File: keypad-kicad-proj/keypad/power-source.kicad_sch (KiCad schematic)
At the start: 12 parts, among them J1 Screw_Terminal_01x02, Q3 IRF9393TRPBF, U2 TLV75901PDRVT

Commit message: footprints
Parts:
- C1, C2: footprint (none) -> Capacitor_SMD:C_0603_1608Metric
- D22: footprint (none) -> Diode_SMD:D_SOD-123
- Q3: footprint SOIC127P600X175-8N -> PUT_RocketLab_other:SOIC127P600X175-8N
- R1: footprint (none) -> Resistor_SMD:R_0402_1005Metric
- R12, R2, R3: footprint (none) -> Resistor_SMD:R_0805_2012Metric
- R4: footprint (none) -> Resistor_SMD:R_0603_1608Metric
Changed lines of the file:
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@@
       (effects (font (size 1.27 1.27)) (justify left))
     )
-    (property "Footprint" "" (at 130.81 125.73 0)
+    (property "Footprint" "Capacitor_SMD:C_0603_1608Metric" (at 130.81 125.73 0)
       (effects (font (size 1.27 1.27)) hide)
     )
@@
       (effects (font (size 1.27 1.27)) (justify left))
     )
-    (property "Footprint" "" (at 173.99 123.19 0)
+    (property "Footprint" "Resistor_SMD:R_0805_2012Metric" (at 173.99 123.19 0)
       (effects (font (size 1.27 1.27)) hide)
     )
@@
       (effects (font (size 1.27 1.27)) (justify left))
     )
-    (property "Footprint" "" (at 182.88 127 0)
+    (property "Footprint" "Capacitor_SMD:C_0603_1608Metric" (at 182.88 127 0)
       (effects (font (size 1.27 1.27)) hide)
     )
@@
       (effects (font (size 1.27 1.27)) (justify left))
     )
-    (property "Footprint" "" (at 134.62 57.15 0)
+    (property "Footprint" "Resistor_SMD:R_0805_2012Metric" (at 134.62 57.15 0)
       (effects (font (size 1.27 1.27)) hide)
     )
@@
       (effects (font (size 1.27 1.27)))
     )
-    (property "Footprint" "SOIC127P600X175-8N" (at 165.1 141.91 0)
+    (property "Footprint" "PUT_RocketLab_other:SOIC127P600X175-8N" (at 165.1 141.91 0)
       (effects (font (size 1.27 1.27)) (justify left top) hide)
     )
@@
       (effects (font (size 1.27 1.27)) (justify left))
     )
-    (property "Footprint" "" (at 134.62 64.77 0)
+    (property "Footprint" "Resistor_SMD:R_0603_1608Metric" (at 134.62 64.77 0)
       (effects (font (size 1.27 1.27)) hide)
     )
@@
       (effects (font (size 1.27 1.27)) (justify left))
     )
-    (property "Footprint" "" (at 173.99 128.27 0)
+    (property "Footprint" "Resistor_SMD:R_0402_1005Metric" (at 173.99 128.27 0)
       (effects (font (size 1.27 1.27)) hide)
     )
@@
       (effects (font (size 1.27 1.27)) (justify right))
     )
-    (property "Footprint" "" (at 172.72 52.07 90)
+    (property "Footprint" "Diode_SMD:D_SOD-123" (at 172.72 52.07 90)
       (effects (font (size 1.27 1.27)) hide)
     )
@@
       (effects (font (size 1.27 1.27)) (justify left))
     )
-    (property "Footprint" "" (at 172.72 63.5 0)
-      (effects (font (size 1.27 1.27)) hide)
-    )
+    (property "Footprint" "Resistor_SMD:R_0805_2012Metric" (at 172.72 63.5 0)
+      (effects (font (size 1.27 1.27)) hide)
+    )

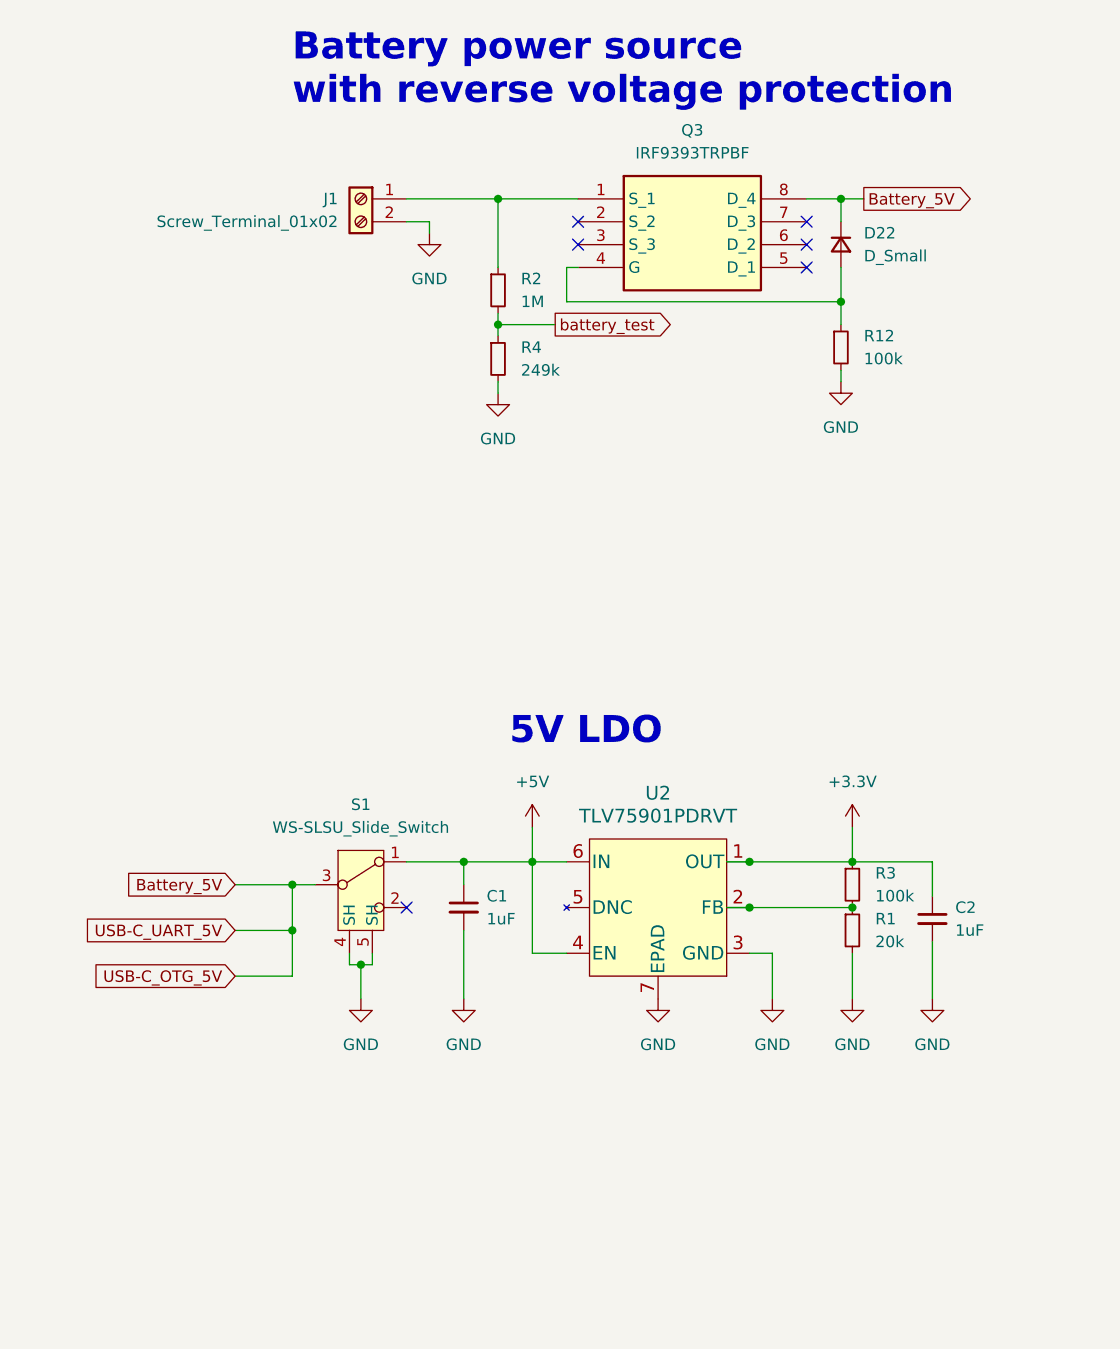
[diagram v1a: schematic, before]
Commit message: add all footprints & move libs to project specific
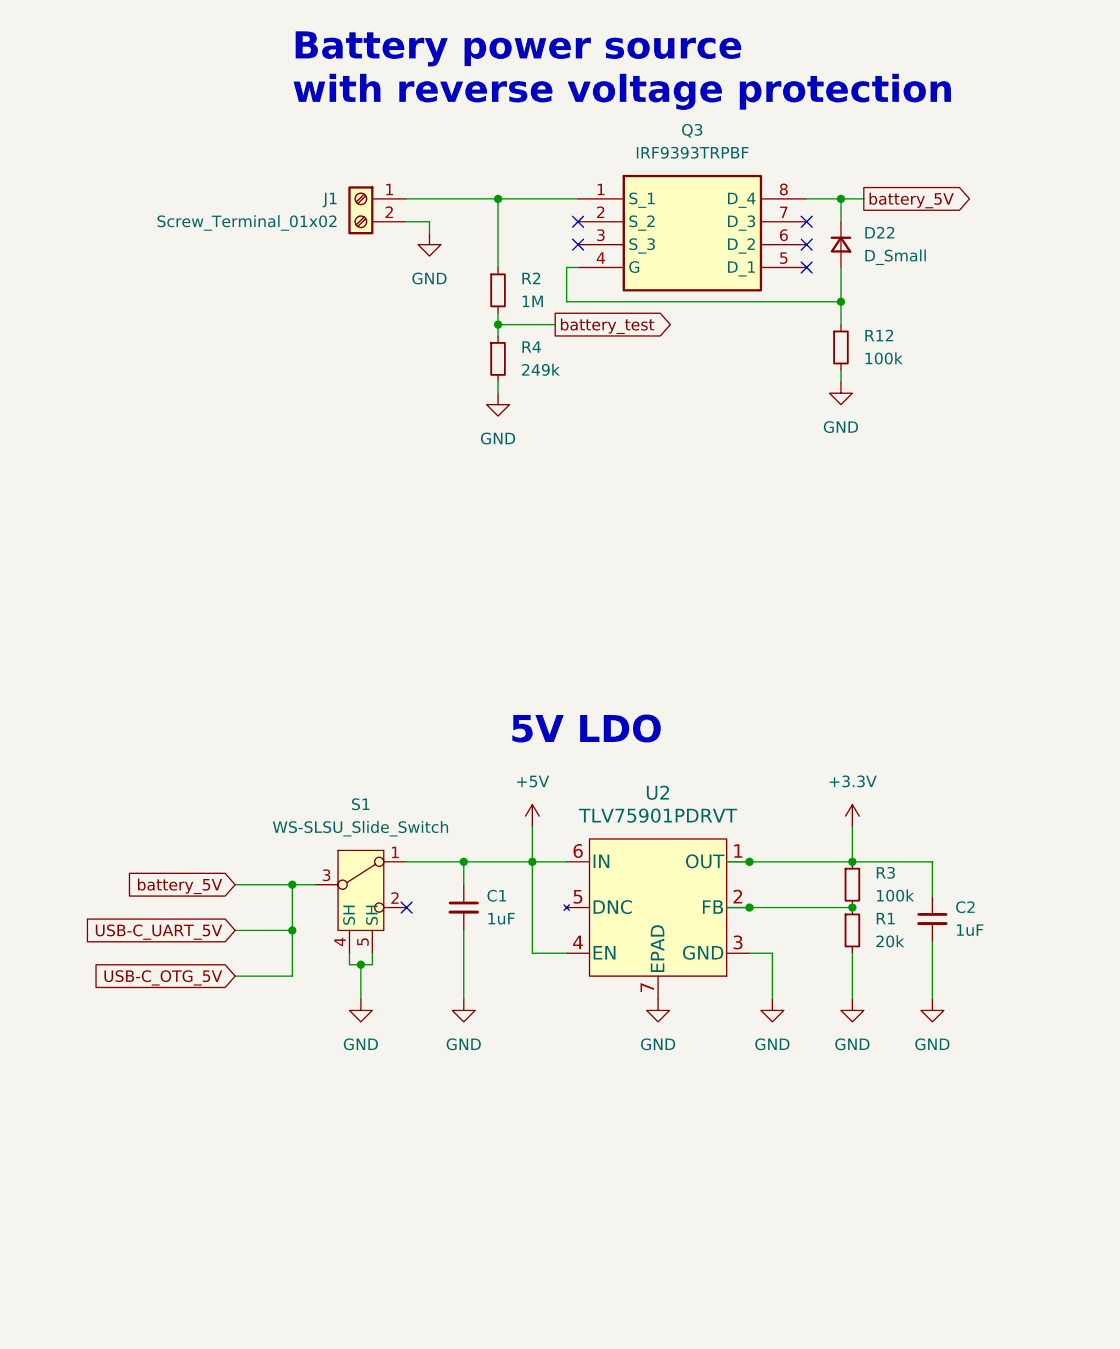
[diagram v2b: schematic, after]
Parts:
- J1: footprint (none) -> PUT_RocketLab_other:XY2500R-DS(5.08)-02V
- S1: footprint (none) -> PUT_RocketLab_other:EG1206A
- U2: footprint DRV6_1X1P6_TEX -> PUT_RocketLab_IC:TLV75901PDRVT
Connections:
- net Battery_5V renamed USB-C_OTG_5V
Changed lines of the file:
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@@
     )
   )
-  (global_label "Battery_5V" (shape input) (at 105.41 123.19 180) (fields_autoplaced)
+  (global_label "battery_5V" (shape input) (at 105.41 123.19 180) (fields_autoplaced)
     (effects (font (size 1.27 1.27)) (justify right))
-    (property "Intersheetrefs" "${INTERSHEET_REFS}" (at 92.4463 123.19 0)
+    (property "Intersheetrefs" "${INTERSHEET_REFS}" (at 92.5673 123.19 0)
       (effects (font (size 1.27 1.27)) (justify right) hide)
     )
@@
     )
   )
-  (global_label "Battery_5V" (shape output) (at 175.26 46.99 0) (fields_autoplaced)
+  (global_label "battery_5V" (shape output) (at 175.26 46.99 0) (fields_autoplaced)
     (effects (font (size 1.27 1.27)) (justify left))
-    (property "Intersheetrefs" "${INTERSHEET_REFS}" (at 188.2237 46.99 0)
+    (property "Intersheetrefs" "${INTERSHEET_REFS}" (at 188.1027 46.99 0)
       (effects (font (size 1.27 1.27)) (justify left) hide)
     )
@@
       (effects (font (size 1.27 1.27)) (justify left))
     )
-    (property "Footprint" "" (at 119.38 46.99 0)
+    (property "Footprint" "PUT_RocketLab_other:XY2500R-DS(5.08)-02V" (at 119.38 46.99 0)
       (effects (font (size 1.27 1.27)) hide)
     )
@@
       (effects (font (size 1.524 1.524)))
     )
-    (property "Footprint" "DRV6_1X1P6_TEX" (at 151.13 116.84 0)
+    (property "Footprint" "PUT_RocketLab_IC:TLV75901PDRVT" (at 151.13 116.84 0)
       (effects (font (size 1.524 1.524)) hide)
     )
-    (property "Datasheet" "" (at 167.64 115.57 0)
-      (effects (font (size 1.524 1.524)))
+    (property "Datasheet" "https://www.ti.com/lit/ds/symlink/tlv759p.pdf?HQS=dis-mous-null-mousermode-dsf-pf-null-wwe&ts=1700306112254&ref_url=https%253A%252F%252Fwww.ti.com%252Fgeneral%252Fdocs%252Fsuppproductinfo.tsp%253FdistId%253D26%2526gotoUrl%253Dhttps%253A%252F%252Fwww.ti.com%252Flit%252Fgpn%252Ftlv759p" (at 167.64 115.57 0)
+      (effects (font (size 1.524 1.524)) hide)
     )
     (pin "1")
@@
       (effects (font (size 1.27 1.27)))
     )
-    (property "Footprint" "" (at 119.38 123.19 0)
-      (effects (font (size 1.27 1.27)) hide)
-    )
+    (property "Footprint" "PUT_RocketLab_other:EG1206A" (at 119.38 123.19 0)
+      (effects (font (size 1.27 1.27)) hide)
+    )

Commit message: main layout
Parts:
- R1: footprint Resistor_SMD:R_0402_1005Metric -> Resistor_SMD:R_0805_2012Metric
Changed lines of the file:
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@@
       (effects (font (size 1.27 1.27)) (justify left))
     )
-    (property "Footprint" "Resistor_SMD:R_0402_1005Metric" (at 173.99 128.27 0)
+    (property "Footprint" "Resistor_SMD:R_0805_2012Metric" (at 173.99 128.27 0)
       (effects (font (size 1.27 1.27)) hide)
     )

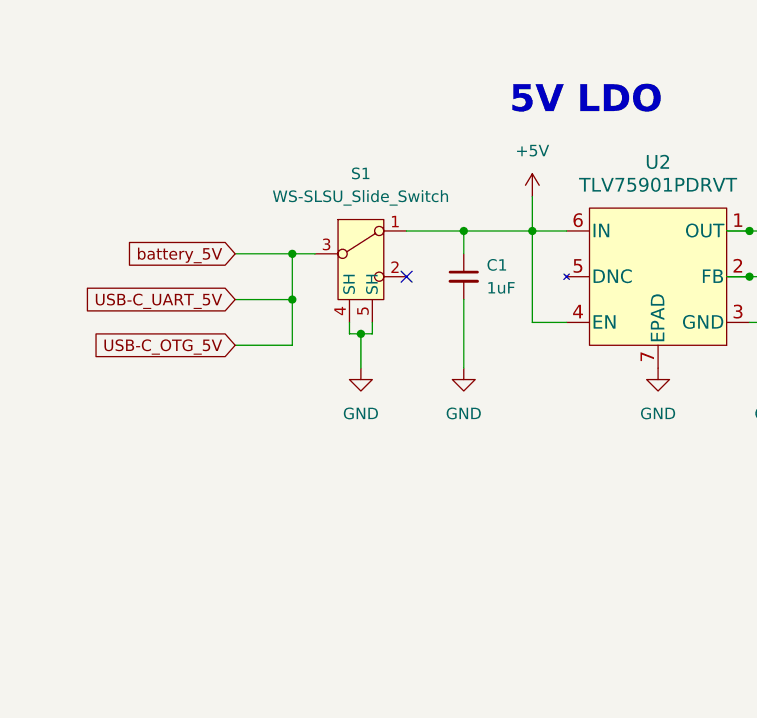
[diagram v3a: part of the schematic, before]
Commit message: small improvements & different connection in power button
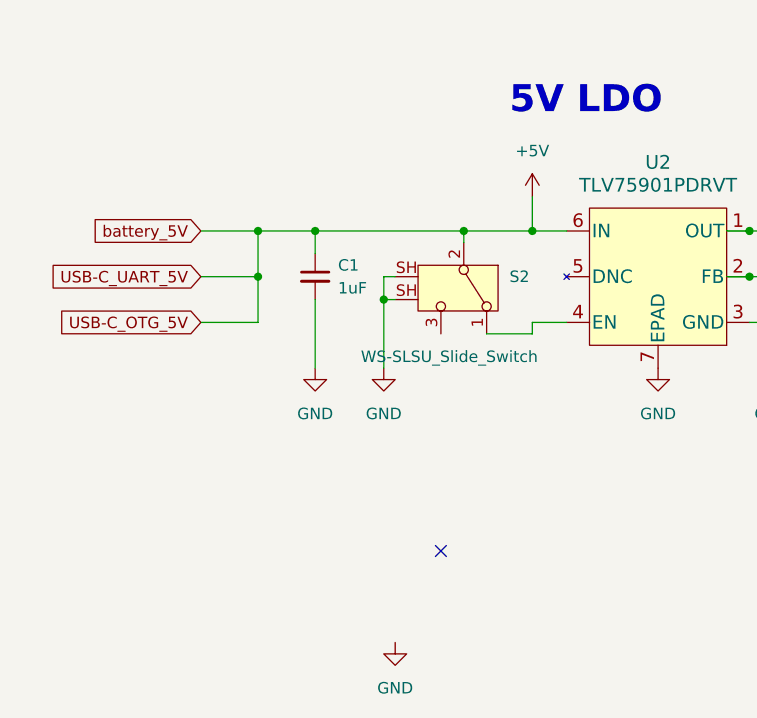
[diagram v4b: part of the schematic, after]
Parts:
- removed S1: WS-SLSU_Slide_Switch, PUT_RocketLab_other:EG1206A, symbol PUT_RocketLab_connectors:WS-SLSU_Slide_Switch
- added S2: WS-SLSU_Slide_Switch, PUT_RocketLab_other:EG1206A, symbol PUT_RocketLab_misc:WS-SLSU_Slide_Switch
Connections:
- net USB-C_OTG_5V is gone; now on net +5V: D22.1 (K), Q3.8 (D_4)
- net +5V: now also S2.2; no longer U2.4 (EN)
- net GND: now also S2.SH
- new net: S2.1, U2.4 (EN)
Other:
- moved on the sheet: C1

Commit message: ldo adjustments
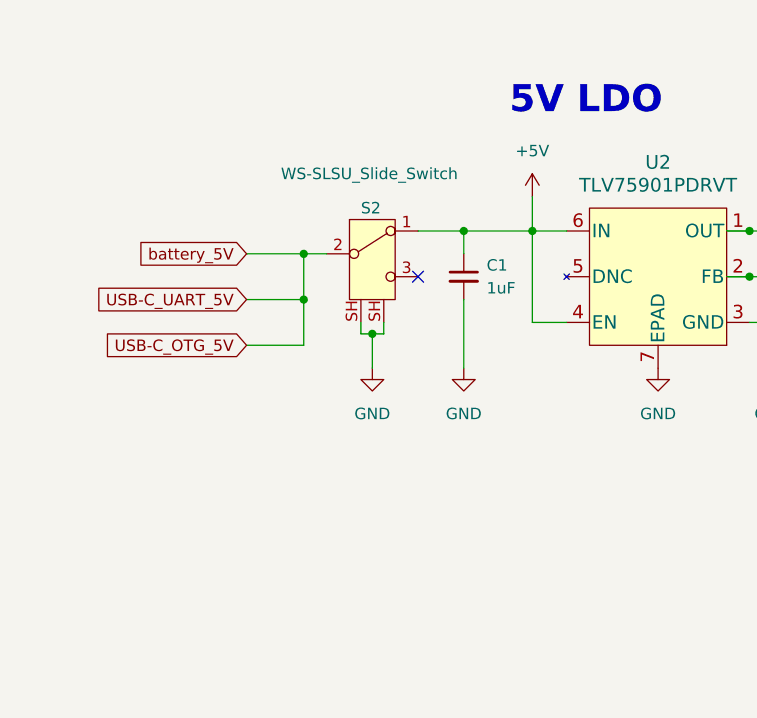
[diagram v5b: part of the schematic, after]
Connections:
- net +5V: now also S2.1, U2.4 (EN); no longer D22.1 (K), Q3.8 (D_4), S2.2
- new net USB-C_OTG_5V: D22.1 (K), Q3.8 (D_4), S2.2
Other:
- moved on the sheet: C1, S2
